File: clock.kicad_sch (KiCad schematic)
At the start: 24 parts, among them P16 SMA, P2 SMA, U19 SI5351C, X1 TCXO

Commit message: Change microcontroller U23 to LPC4330FET180
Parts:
- removed R22: 33, Resistor_SMD:R_0402_1005Metric, symbol Device:R
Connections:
- net CLK6: no longer names the net of U19.16 (CLK6)
- no-connect marks 3 -> 4
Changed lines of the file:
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@@
+	)
+	(no_connect
+		(at 165.1 91.44)
 	)
 	(no_connect
@@
 	(wire
 		(pts
-			(xy 170.18 91.44) (xy 170.18 104.14)
-		)
-		(stroke
-			(width 0)
-			(type default)
-		)
-	)
-	(wire
-		(pts
 			(xy 165.1 60.96) (xy 182.88 60.96)
 		)
@@
 	(wire
 		(pts
-			(xy 170.18 104.14) (xy 182.88 104.14)
-		)
-		(stroke
-			(width 0)
-			(type default)
-		)
-	)
-	(wire
-		(pts
 			(xy 190.5 93.98) (xy 191.77 93.98)
 		)
@@
 	(wire
 		(pts
-			(xy 190.5 104.14) (xy 191.77 104.14)
-		)
-		(stroke
-			(width 0)
-			(type default)
-		)
-	)
-	(wire
-		(pts
 			(xy 132.08 120.65) (xy 115.57 120.65)
 		)
@@
 		(pts
 			(xy 128.27 43.18) (xy 129.54 43.18)
-		)
-		(stroke
-			(width 0)
-			(type default)
-		)
-	)
-	(wire
-		(pts
-			(xy 165.1 91.44) (xy 170.18 91.44)
 		)
 		(stroke
@@
 	(label "OEB"
 		(at 118.11 120.65 0)
-		(fields_autoplaced yes)
-		(effects
-			(font
-				(size 1.524 1.524)
-			)
-			(justify left bottom)
-		)
-	)
-	(label "CLK6"
-		(at 176.53 104.14 0)
 		(fields_autoplaced yes)
 		(effects
@@
 		)
 	)
-	(hierarchical_label "AUX_CLK"
-		(shape output)
-		(at 191.77 104.14 0)
-		(fields_autoplaced yes)
-		(effects
-			(font
-				(size 1.524 1.524)
-			)
-			(justify left)
-		)
-	)
 	(hierarchical_label "CLKOUT"
 		(shape output)
@@
 		)
 	)
-	(symbol
-		(lib_id "Device:R")
-		(at 186.69 104.14 270)
-		(unit 1)
-		(exclude_from_sim no)
-		(in_bom yes)
-		(on_board yes)
-		(dnp no)
-		(fields_autoplaced yes)
-		(property "Reference" "R22"
-			(at 186.69 97.79 90)
-			(effects
-				(font
-					(size 1.27 1.27)
-				)
-			)
-		)
-		(property "Value" "33"
-			(at 186.69 100.33 90)
-			(effects
-				(font
-					(size 1.27 1.27)
-				)
-			)
-		)
-		(property "Footprint" "Resistor_SMD:R_0402_1005Metric"
-			(at 186.69 104.14 0)
-			(effects
-				(font
-					(size 1.524 1.524)
-				)
-				(hide yes)
-			)
-		)
-		(property "Datasheet" "~"
-			(at 186.69 104.14 0)
-			(effects
-				(font
-					(size 1.524 1.524)
-				)
-				(hide yes)
-			)
-		)
-		(property "Description" "RES 33 OHM 5% 1/16W 0402"
-			(at 186.69 104.14 0)
-			(effects
-				(font
-					(size 1.524 1.524)
-				)
-				(hide yes)
-			)
-		)
-		(property "Manufacturer" "Yageo"
-			(at 186.69 104.14 0)
-			(effects
-				(font
-					(size 1.524 1.524)
-				)
-				(hide yes)
-			)
-		)
-		(property "Part Number" "RC0402JR-0733RL"
-			(at 186.69 104.14 0)
-			(effects
-				(font
-					(size 1.524 1.524)
-				)
-				(hide yes)
-			)
-		)
-		(property "Substitution" "any equivalent"
-			(at 186.69 104.14 0)
-			(effects
-				(font
-					(size 1.27 1.27)
-				)
-				(hide yes)
-			)
-		)
-		(pin "1"
-		)
-		(pin "2"
-		)
-		(instances
-			(project "praline"
-				(path "/dba4afc6-760f-46cb-a936-032b76448f03/82363729-914a-4be2-9abc-c6e1e42dff36"
-					(reference "R22")
-					(unit 1)
-				)
-			)
-		)
-	)

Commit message: Increase outermost DC block to 25 V
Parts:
- C113, C119, C120, C121, C122, C168: Part Number CL05A105KP5NNNC -> CL05A105KA5NQNC; Substitution Taiyo Yuden LMK105BJ105KV-F -> Murata GRM155R61E105KA12D
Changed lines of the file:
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@@
 			)
 		)
-		(property "Description" "CAP CER 1UF 10V X5R 0402"
+		(property "Description" "CAP CER 1UF 25V X5R 0402"
 			(at 173.99 142.24 0)
 			(effects
@@
 			)
 		)
-		(property "Part Number" "CL05A105KP5NNNC"
+		(property "Part Number" "CL05A105KA5NQNC"
 			(at 173.99 142.24 0)
 			(effects
@@
 			)
 		)
-		(property "Substitution" "Taiyo Yuden LMK105BJ105KV-F"
+		(property "Substitution" "Murata GRM155R61E105KA12D"
 			(at 173.99 142.24 0)
 			(effects
@@
 			)
 		)
-		(property "Description" "CAP CER 1UF 10V X5R 0402"
+		(property "Description" "CAP CER 1UF 25V X5R 0402"
 			(at 163.83 142.24 0)
 			(effects
@@
 			)
 		)
-		(property "Part Number" "CL05A105KP5NNNC"
+		(property "Part Number" "CL05A105KA5NQNC"
 			(at 163.83 142.24 0)
 			(effects
@@
 			)
 		)
-		(property "Substitution" "Taiyo Yuden LMK105BJ105KV-F"
+		(property "Substitution" "Murata GRM155R61E105KA12D"
 			(at 163.83 142.24 0)
 			(effects
@@
 			)
 		)
-		(property "Description" "CAP CER 1UF 10V X5R 0402"
+		(property "Description" "CAP CER 1UF 25V X5R 0402"
 			(at 143.51 142.24 0)
 			(effects
@@
 			)
 		)
-		(property "Part Number" "CL05A105KP5NNNC"
+		(property "Part Number" "CL05A105KA5NQNC"
 			(at 143.51 142.24 0)
 			(effects
@@
 			)
 		)
-		(property "Substitution" "Taiyo Yuden LMK105BJ105KV-F"
+		(property "Substitution" "Murata GRM155R61E105KA12D"
 			(at 143.51 142.24 0)
 			(effects
@@
 			)
 		)
-		(property "Description" "CAP CER 1UF 10V X5R 0402"
+		(property "Description" "CAP CER 1UF 25V X5R 0402"
 			(at 153.67 142.24 0)
 			(effects
@@
 			)
 		)
-		(property "Part Number" "CL05A105KP5NNNC"
+		(property "Part Number" "CL05A105KA5NQNC"
 			(at 153.67 142.24 0)
 			(effects
@@
 			)
 		)
-		(property "Substitution" "Taiyo Yuden LMK105BJ105KV-F"
+		(property "Substitution" "Murata GRM155R61E105KA12D"
 			(at 153.67 142.24 0)
 			(effects
@@
 			)
 		)
-		(property "Description" "CAP CER 1UF 10V X5R 0402"
+		(property "Description" "CAP CER 1UF 25V X5R 0402"
 			(at 184.15 142.24 0)
 			(effects
@@
 			)
 		)
-		(property "Part Number" "CL05A105KP5NNNC"
+		(property "Part Number" "CL05A105KA5NQNC"
 			(at 184.15 142.24 0)
 			(effects
@@
 			)
 		)
-		(property "Substitution" "Taiyo Yuden LMK105BJ105KV-F"
+		(property "Substitution" "Murata GRM155R61E105KA12D"
 			(at 184.15 142.24 0)
 			(effects
@@
 			)
 		)
-		(property "Description" "CAP CER 1UF 10V X5R 0402"
+		(property "Description" "CAP CER 1UF 25V X5R 0402"
 			(at 86.36 43.18 0)
 			(effects
@@
 			)
 		)
-		(property "Part Number" "CL05A105KP5NNNC"
+		(property "Part Number" "CL05A105KA5NQNC"
 			(at 86.36 43.18 0)
 			(effects
@@
 			)
 		)
-		(property "Substitution" "Taiyo Yuden LMK105BJ105KV-F"
+		(property "Substitution" "Murata GRM155R61E105KA12D"
 			(at 86.36 43.18 0)
 			(effects

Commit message: Add more expansion pins
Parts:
- added R84: 33, Resistor_SMD:R_0402_1005Metric, symbol Device:R
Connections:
- net CLK6: now reaches U19.16 (CLK6)
- net CLK6: now also R84.2
- new net AUX_CLK: R84.1
- no-connect marks 4 -> 3
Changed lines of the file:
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@@
 	)
 	(no_connect
-		(at 165.1 91.44)
-	)
-	(no_connect
 		(at 165.1 71.12)
 	)
@@
 	(wire
 		(pts
+			(xy 170.18 91.44) (xy 170.18 104.14)
+		)
+		(stroke
+			(width 0)
+			(type default)
+		)
+	)
+	(wire
+		(pts
+			(xy 190.5 104.14) (xy 191.77 104.14)
+		)
+		(stroke
+			(width 0)
+			(type default)
+		)
+	)
+	(wire
+		(pts
 			(xy 85.09 73.66) (xy 85.09 71.12)
 		)
@@
 	(wire
 		(pts
+			(xy 170.18 104.14) (xy 182.88 104.14)
+		)
+		(stroke
+			(width 0)
+			(type default)
+		)
+	)
+	(wire
+		(pts
 			(xy 78.74 74.93) (xy 78.74 73.66)
 		)
@@
 	(wire
 		(pts
+			(xy 165.1 91.44) (xy 170.18 91.44)
+		)
+		(stroke
+			(width 0)
+			(type default)
+		)
+	)
+	(wire
+		(pts
 			(xy 147.32 54.61) (xy 149.86 54.61)
 		)
@@
 		)
 	)
+	(label "CLK6"
+		(at 176.53 104.14 0)
+		(fields_autoplaced yes)
+		(effects
+			(font
+				(size 1.524 1.524)
+			)
+			(justify left bottom)
+		)
+	)
 	(global_label "SDA"
 		(shape input)
@@
 		)
 	)
+	(hierarchical_label "AUX_CLK"
+		(shape output)
+		(at 191.77 104.14 0)
+		(fields_autoplaced yes)
+		(effects
+			(font
+				(size 1.524 1.524)
+			)
+			(justify left)
+		)
+	)
 	(hierarchical_label "CLKIN"
 		(shape input)
@@
 					(unit 1)
 				)
+			)
+		)
+	)
+	(symbol
+		(lib_id "Device:R")
+		(at 186.69 104.14 270)
+		(unit 1)
+		(exclude_from_sim no)
+		(in_bom yes)
+		(on_board yes)
+		(dnp no)
+		(fields_autoplaced yes)
+		(property "Reference" "R84"
+			(at 186.69 97.79 90)
+			(effects
+				(font
+					(size 1.27 1.27)
+				)
+			)
+		)
+		(property "Value" "33"
+			(at 186.69 100.33 90)
+			(effects
+				(font
+					(size 1.27 1.27)
+				)
+			)
+		)
+		(property "Footprint" "Resistor_SMD:R_0402_1005Metric"
+			(at 186.69 104.14 0)
+			(effects
+				(font
+					(size 1.524 1.524)
+				)
+				(hide yes)
+			)
+		)
+		(property "Datasheet" "~"
+			(at 186.69 104.14 0)
+			(effects
+				(font
+					(size 1.524 1.524)
+				)
+				(hide yes)
+			)
+		)
+		(property "Description" "RES 33 OHM 5% 1/16W 0402"
+			(at 186.69 104.14 0)
+			(effects
+				(font
+					(size 1.524 1.524)
+				)
+				(hide yes)
+			)
+		)
+		(property "Manufacturer" "Yageo"
+			(at 186.69 104.14 0)
+			(effects
+				(font
+					(size 1.524 1.524)
+				)
+				(hide yes)
+			)
+		)
+		(property "Part Number" "RC0402JR-0733RL"
+			(at 186.69 104.14 0)
+			(effects
+				(font
+					(size 1.524 1.524)
+				)
+				(hide yes)
+			)
+		)
+		(property "Substitution" "any equivalent"
+			(at 186.69 104.14 0)
+			(effects
+				(font
+					(size 1.27 1.27)
+				)
+				(hide yes)
+			)
+		)
+		(pin "1"
+		)
+		(pin "2"
+		)
+		(instances
+			(project "praline"
+				(path "/dba4afc6-760f-46cb-a936-032b76448f03/82363729-914a-4be2-9abc-c6e1e42dff36"
+					(reference "R84")
+					(unit 1)
+				)

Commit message: Rearrange RF section
- Use DPDT RF switches to reduce long tracks
- Add limiter
- Add switch control logic
- Move ADC/DAC U18 to RF area
- Remove baseband header P9
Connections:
- net MIX_CLK: now also R23.1; no longer R32.1
- net XCVR_CLK: now also R32.1; no longer R23.1
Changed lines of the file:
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@@
 	(hierarchical_label "XCVR_CLK"
 		(shape output)
-		(at 191.77 93.98 0)
+		(at 191.77 83.82 0)
 		(fields_autoplaced yes)
 		(effects
@@
 	(hierarchical_label "MIX_CLK"
 		(shape output)
-		(at 191.77 83.82 0)
+		(at 191.77 93.98 0)
 		(fields_autoplaced yes)
 		(effects

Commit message: Change SMA connectors to A-SMA-KE-16.5A
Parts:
- P16, P2: footprint praline:Linx_SMA_CONSMA003.062 -> praline:SMA_MyAntenna_A-SMA-KE-16.5A_EdgeMount; Manufacturer TE Connectivity Linx -> MyAntenna; Part Number CONSMA003.062 -> A-SMA-KE-16.5A
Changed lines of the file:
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@@
 			)
 		)
-		(property "Footprint" "praline:Linx_SMA_CONSMA003.062"
+		(property "Footprint" "praline:SMA_MyAntenna_A-SMA-KE-16.5A_EdgeMount"
 			(at 69.85 73.66 0)
 			(effects
@@
 			)
 		)
-		(property "Manufacturer" "TE Connectivity Linx"
+		(property "Manufacturer" "MyAntenna"
 			(at 69.85 73.66 0)
 			(effects
@@
 			)
 		)
-		(property "Part Number" "CONSMA003.062"
+		(property "Part Number" "A-SMA-KE-16.5A"
 			(at 69.85 73.66 0)
 			(effects
@@
 			)
 		)
-		(property "Footprint" "praline:Linx_SMA_CONSMA003.062"
+		(property "Footprint" "praline:SMA_MyAntenna_A-SMA-KE-16.5A_EdgeMount"
 			(at 217.17 73.66 0)
 			(effects
@@
 			)
 		)
-		(property "Manufacturer" "TE Connectivity Linx"
+		(property "Manufacturer" "MyAntenna"
 			(at 217.17 73.66 0)
 			(effects
@@
 			)
 		)
-		(property "Part Number" "CONSMA003.062"
+		(property "Part Number" "A-SMA-KE-16.5A"
 			(at 217.17 73.66 0)
 			(effects

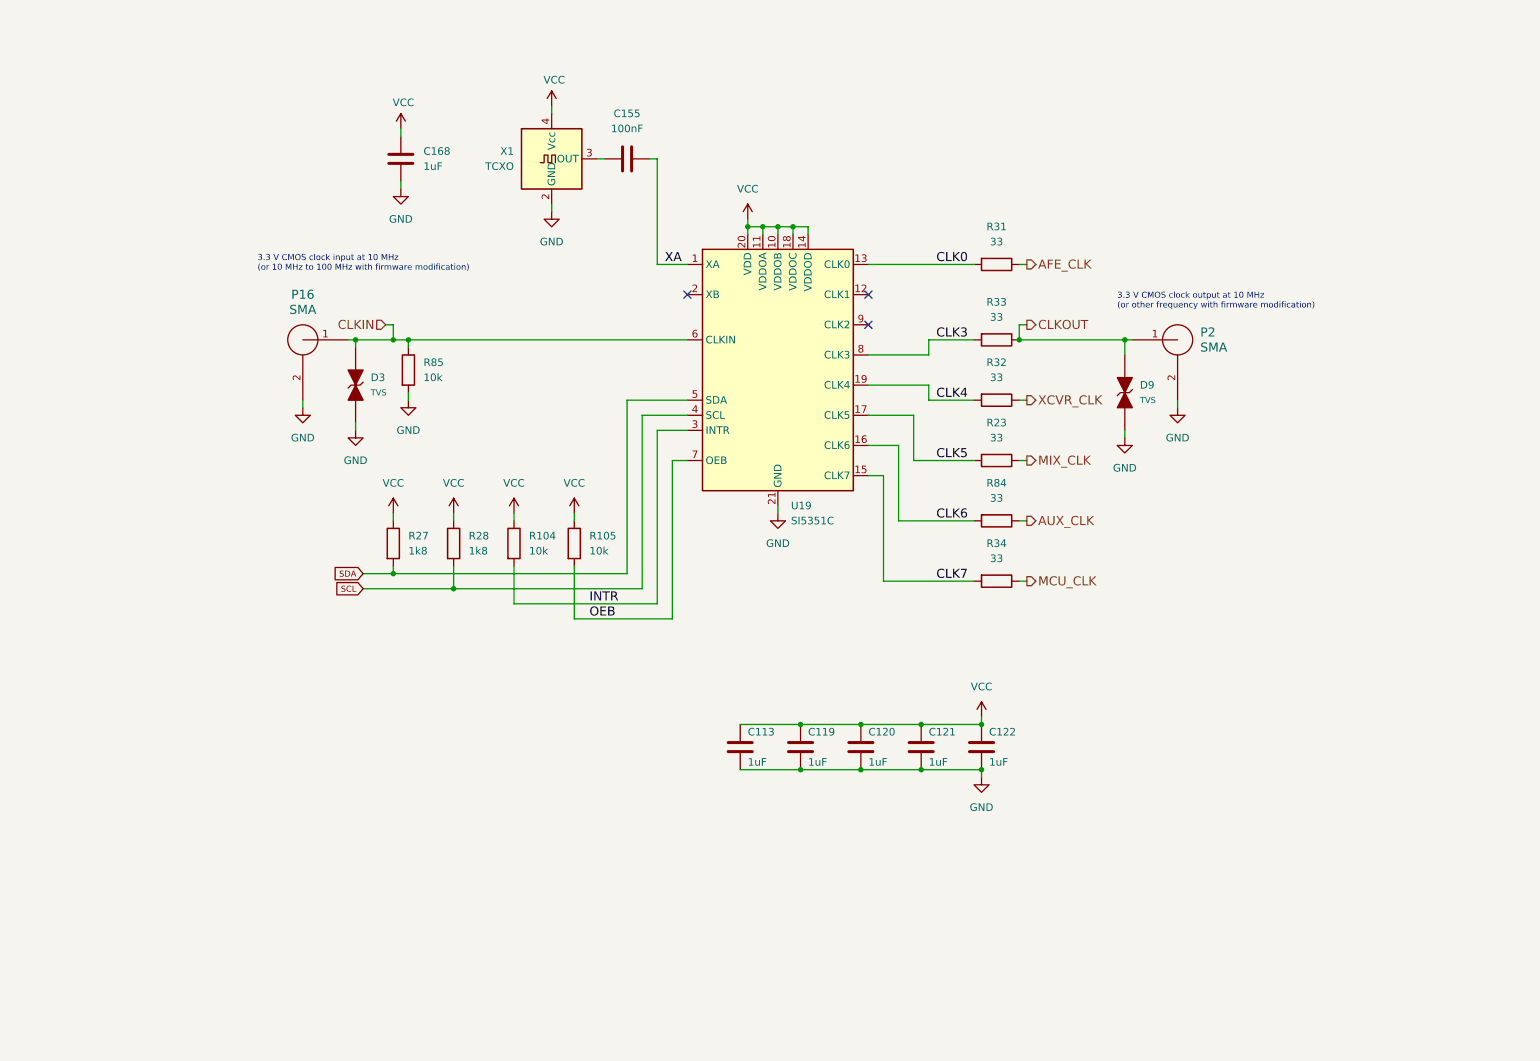
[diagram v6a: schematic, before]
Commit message: Multiplex clock I/O signals
- Allow switching of CLKIN and CLKOUT ports to trigger I/O and other signals
- Add SCT_CLK
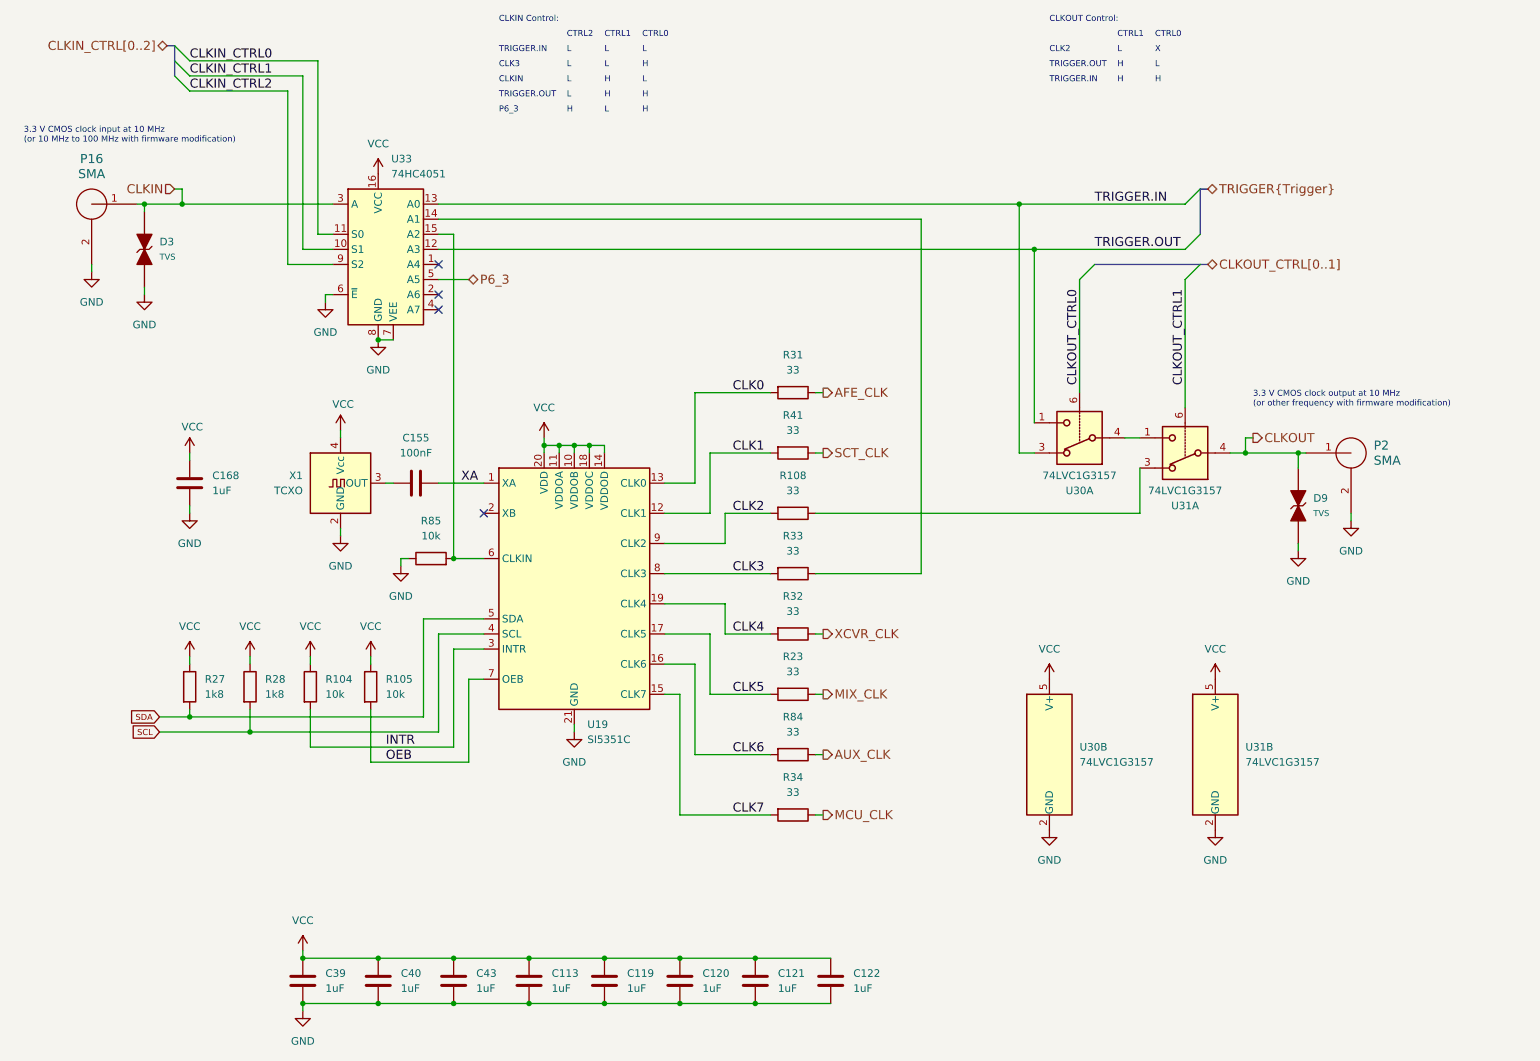
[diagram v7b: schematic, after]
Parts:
- added C39, C40, C43: 1uF, Capacitor_SMD:C_0402_1005Metric, symbol Device:C
- added R108, R41: 33, Resistor_SMD:R_0402_1005Metric, symbol Device:R
- added U30, U31: 74LVC1G3157, Package_TO_SOT_SMD:SOT-363_SC-70-6, symbol Analog_Switch:NC7SB3157P6X
- added U33: 74HC4051, Package_DFN_QFN:DHVQFN-16-1EP_2.5x3.5mm_P0.5mm_EP1x2mm, symbol 74xx:74HC4051
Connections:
- net CLKIN: now also U33.3 (A); no longer R85.1, U19.6 (CLKIN)
- net CLKOUT: now also U31.4; no longer R33.1
- net GND: now also R85.1, C39.2, C40.2, C43.2, U30.2 (GND), U31.2 (GND), U33.6 (~{E}), U33.7 (VEE), U33.8 (GND); no longer R85.2
- net VCC: now also C39.1, C40.1, C43.1, U30.5 (V+), U31.5 (V+), U33.16 (VCC)
- net CLK1: now reaches U19.12 (CLK1)
- net CLK1: now also R41.2
- net CLK2: now reaches U19.9 (CLK2)
- net CLK2: now also R108.2
- new net: R85.2, U19.6 (CLKIN), U33.15 (A2)
- new net: U30.4, U31.1
- new net: R33.1, U33.14 (A1)
- new net: R108.1, U31.3
- new net CLKIN_CTRL0: U33.11 (S0)
- new net CLKIN_CTRL1: U33.10 (S1)
- new net CLKIN_CTRL2: U33.9 (S2)
- new net CLKOUT_CTRL0: U30.6
- new net CLKOUT_CTRL1: U31.6
- new net P6_3: U33.5 (A5)
- new net SCT_CLK: R41.1
- new net TRIGGER.IN: U30.3, U33.13 (A0)
- new net TRIGGER.OUT: U30.1, U33.12 (A3)
- no-connect marks 3 -> 4
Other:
- note added: "CLK2"
- note added: "CLK3"
- note added: "CLKIN"
- note added: "CLKIN Control:"
- note added: "CLKOUT Control:"
- note added: "CTRL0"
- note added: "CTRL1"
- note added: "CTRL2"
- note added: "H"
- note added: "L"
- note added: "P6_3"
- note added: "TRIGGER.IN"
- note added: "TRIGGER.OUT"
- note added: "X"
- moved on the sheet: C113, C119, C120, C121, C122, C155, C168, D3, D9, P16, P2, R104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

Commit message: Connect mixer U4 LD and ENBL pins to MCU
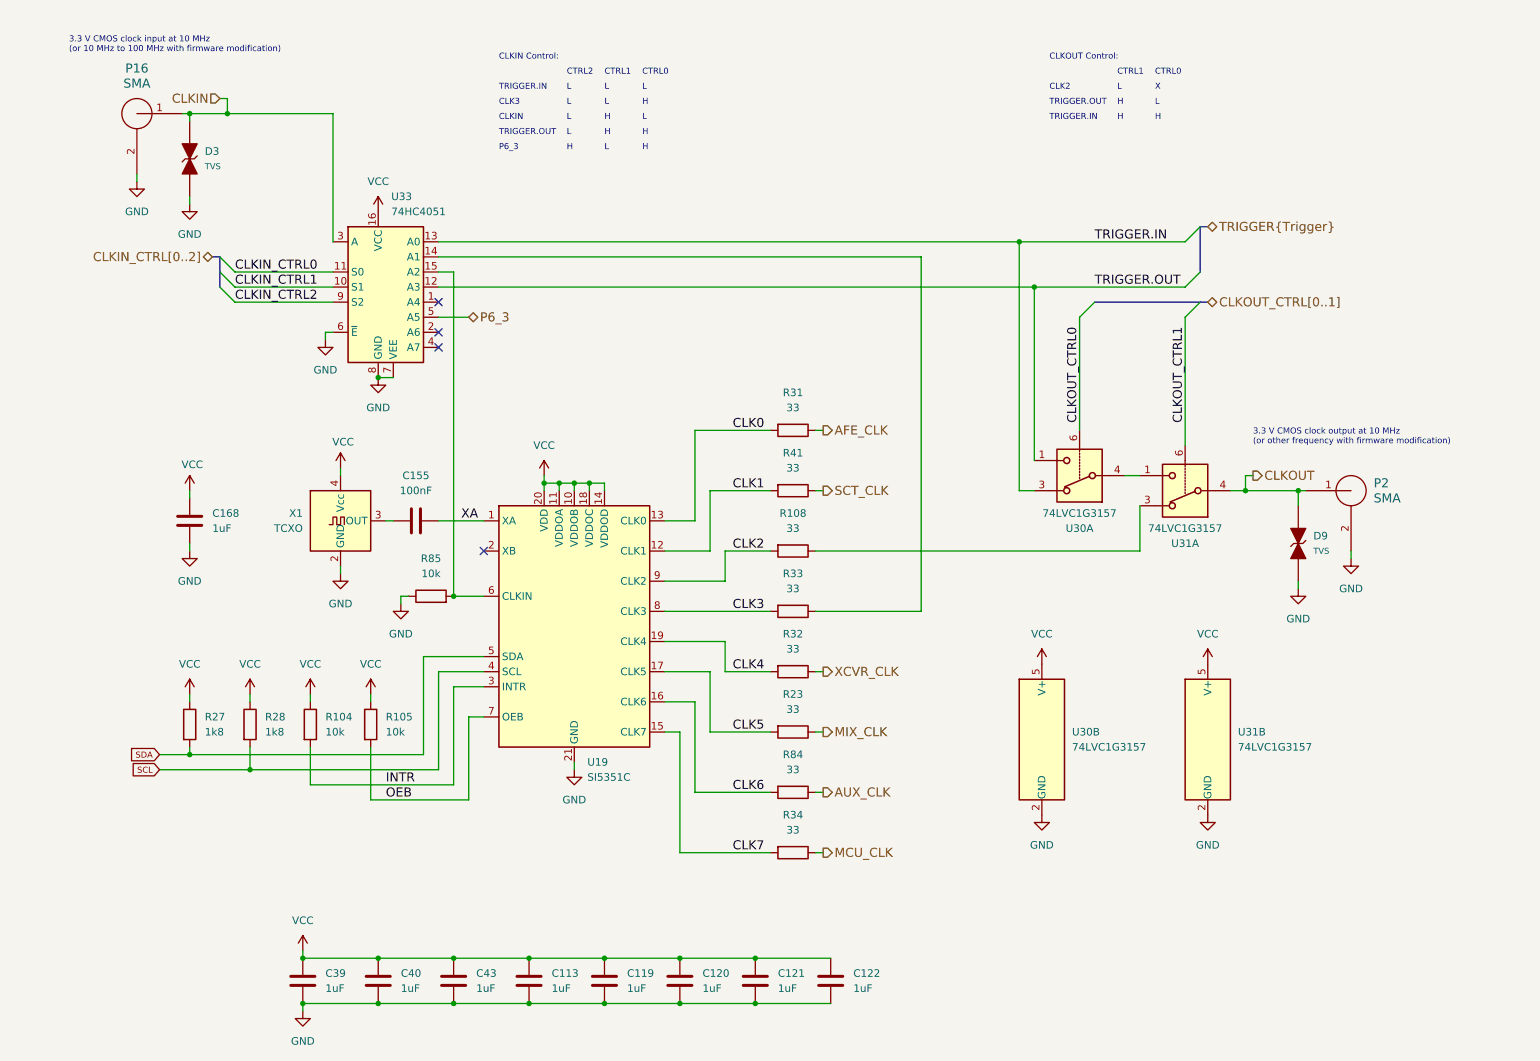
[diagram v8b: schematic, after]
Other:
- moved on the sheet: C155, C168, D3, D9, P16, P2, R104, R105, R108, R23, R27, R28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
